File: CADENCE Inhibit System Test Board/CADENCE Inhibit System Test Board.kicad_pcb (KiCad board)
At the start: 2 copper layers, 70 x 95 mm, 61 parts, among them IC1 LTC7004IMSE#WTRPBF, IC2 LTC7004IMSE#WTRPBF, IC3 LTC7004IMSE#WTRPBF, IC4 LTC7004IMSE#WTRPBF, IC5 LTC7004IMSE#WTRPBF, J1 INHIBIT_P2, J10 Conn_01x04, J11 Conn_01x02, J2 INHIBIT_P2, J3 INHIBIT_P2, J4 INHIBIT_P2, J5 INHIBIT_P2, J6 INHIBIT_P2, J7 INHIBIT_P2, J8 INHIBIT_P2, J9 INHIBIT_P2, Q1 SUD23N06-31-GE3, Q2 SUD23N06-31-GE3, Q3 SUD23N06-31-GE3, Q4 SUD23N06-31-GE3, Q5 SUD23N06-31-GE3, Q6 SUD23N06-31-GE3, Q7 SUD23N06-31-GE3, U1 MIC4427YM-TR, U2 MIC4427YM-TR

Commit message: made pcb smaller
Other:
- board size 70 x 95 mm -> 70 x 68.6 mm
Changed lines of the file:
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@@
 		)
 		(property "Value" "LTC7004IMSE#WTRPBF"
-			(at 1.5 -0.24 90)
+			(at -0.6556 -0.24 90)
 			(unlocked yes)
 			(layer "F.Fab")
@@
 		(tags "connector Hirose DF11 vertical")
 		(property "Reference" "J5"
-			(at 1 -4.2 90)
+			(at 1 -2.5 90)
 			(layer "F.SilkS")
 			(effects
@@
 		(tags "connector Hirose DF11 vertical")
 		(property "Reference" "J1"
-			(at 6.9652 -30.2127 90)
+			(at 1 -2.5 90)
 			(layer "F.SilkS")
 			(effects
@@
 	(gr_rect
 		(start 120.465637 42.411896)
-		(end 190.465637 137.411896)
+		(end 190.465637 111)
 		(stroke
 			(width 0.2)

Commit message: mounting holes added
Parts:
- added H1: MountingHole, MountingHole:MountingHole_3.2mm_M3, F.Cu at (124.5, 43.0)
- added H2: MountingHole, MountingHole:MountingHole_3.2mm_M3, F.Cu at (186.5, 43.5)
- added H3: MountingHole, MountingHole:MountingHole_3.2mm_M3, F.Cu at (193.5, 113.0)
- added H4: MountingHole, MountingHole:MountingHole_3.2mm_M3, F.Cu at (125.0, 106.5)
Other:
- board size 70 x 68.6 mm -> 70 x 72.5 mm

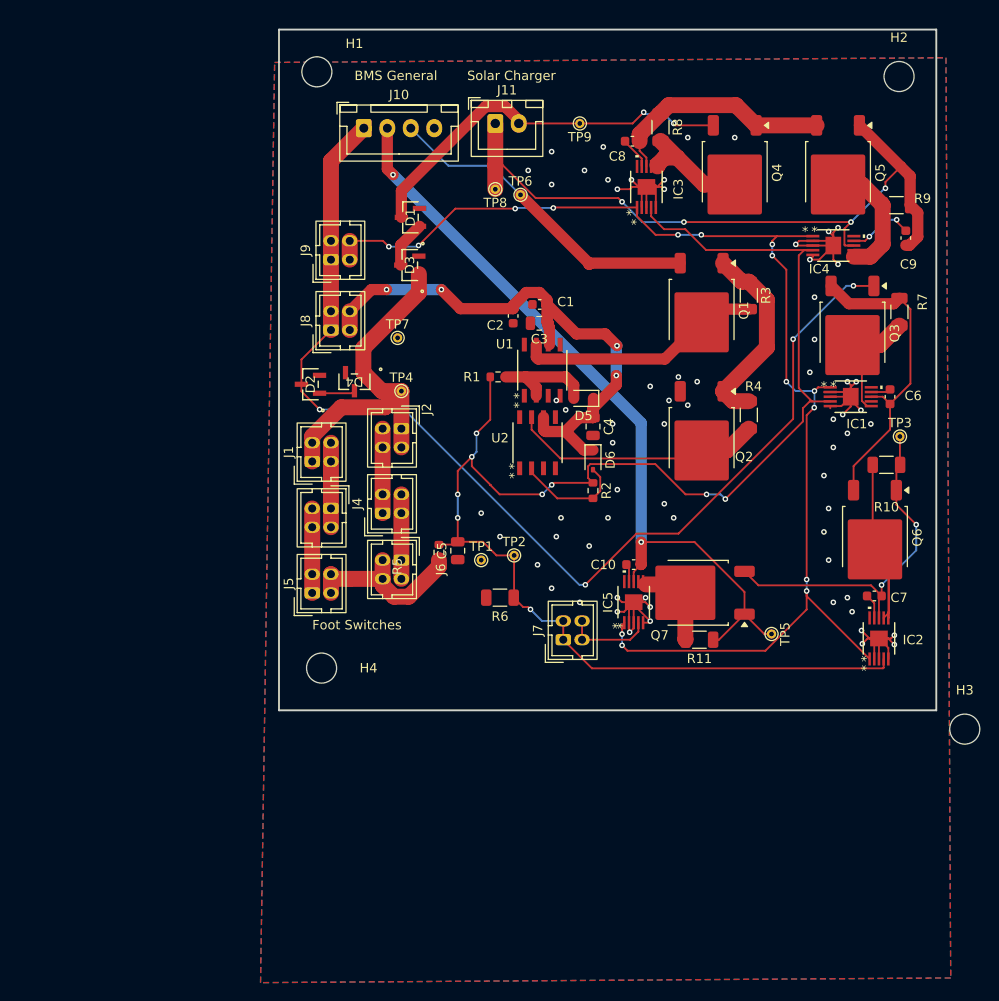
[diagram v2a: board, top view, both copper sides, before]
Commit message: moved parts and updated mounting holes
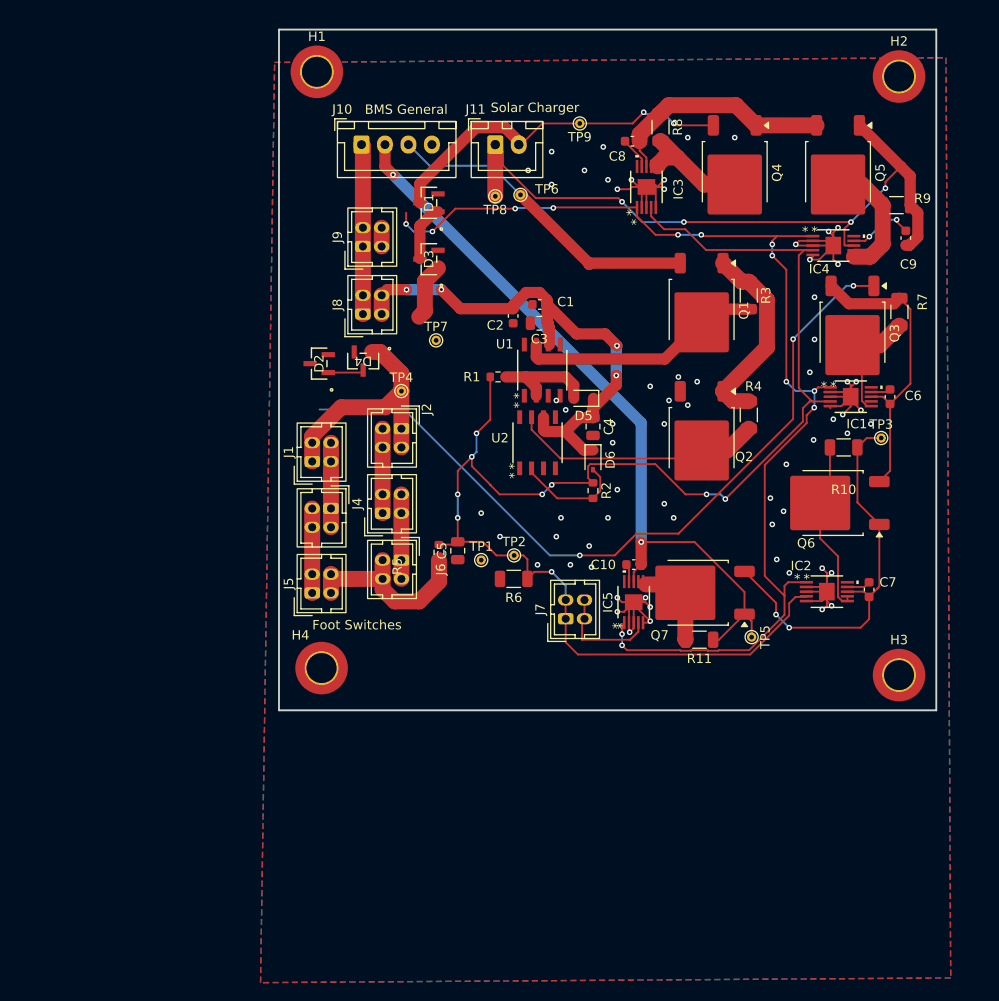
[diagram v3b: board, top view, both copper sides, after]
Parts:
- H1, H2, H3, H4: value MountingHole -> MountingHole_Pad; footprint MountingHole:MountingHole_3.2mm_M3 -> MountingHole:MountingHole_3.2mm_M3_DIN965_Pad_TopOnly
- moved H3 9.06 mm to (186.5, 107.2)
- moved IC2 7.46 mm to (178.8, 98.4), turned to 0 degrees
- moved Q6 5.87 mm to (179.4, 88.9), turned to 180 degrees
- moved R10 4.92 mm to (180.6, 83.0)
- moved TP7 4.11 mm to (137.2, 71.6)
- moved J8 3.80 mm to (129.4, 68.8)
- moved J9 3.68 mm to (129.4, 61.6)
- moved D1 2.50 mm to (136.4, 57.0)
- moved R6 2.48 mm to (145.5, 97.0)
- moved D4 2.39 mm to (129.4, 73.8)
- moved D2 2.39 mm to (124.7, 74.1)
- moved J11 2.25 mm to (143.5, 50.8)
- moved J7 2.25 mm to (151.0, 101.2)
- moved TP5 2.15 mm to (170.8, 103.2)
- moved D3 2.13 mm to (136.4, 63.0)
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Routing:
- net Cell 1+: track 118.4 -> 100.5 mm, vias 4 -> 3
- net HIGH_SIDE_PWR: track 134.6 -> 123.4 mm, vias 15 -> 13
- net Net-(D3-K): track 38.0 -> 32.1 mm
- net EN: track 164.7 -> 159.9 mm
- net Net-(IC2-TS): track 37.8 -> 42.1 mm
- net LOW_SIDE_PWR: track 62.0 -> 57.9 mm
- net V_mppt_i: track 41.8 -> 38.7 mm
- net Net-(IC2-TGDN): track 23.1 -> 20.1 mm
- net UNREG: track 83.6 -> 81.0 mm
- net Net-(IC1-TS): track 34.9 -> 32.9 mm
- net Net-(IC5-INP): track 9.30 -> 11.3 mm
- net Net-(J5-Pin_2): track 18.9 -> 20.5 mm
- net Net-(D1-K): track 4.96 -> 6.02 mm
- net VSS: track 82.0 -> 82.9 mm, vias 67 -> 66

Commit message: edited layout and rerouted traces
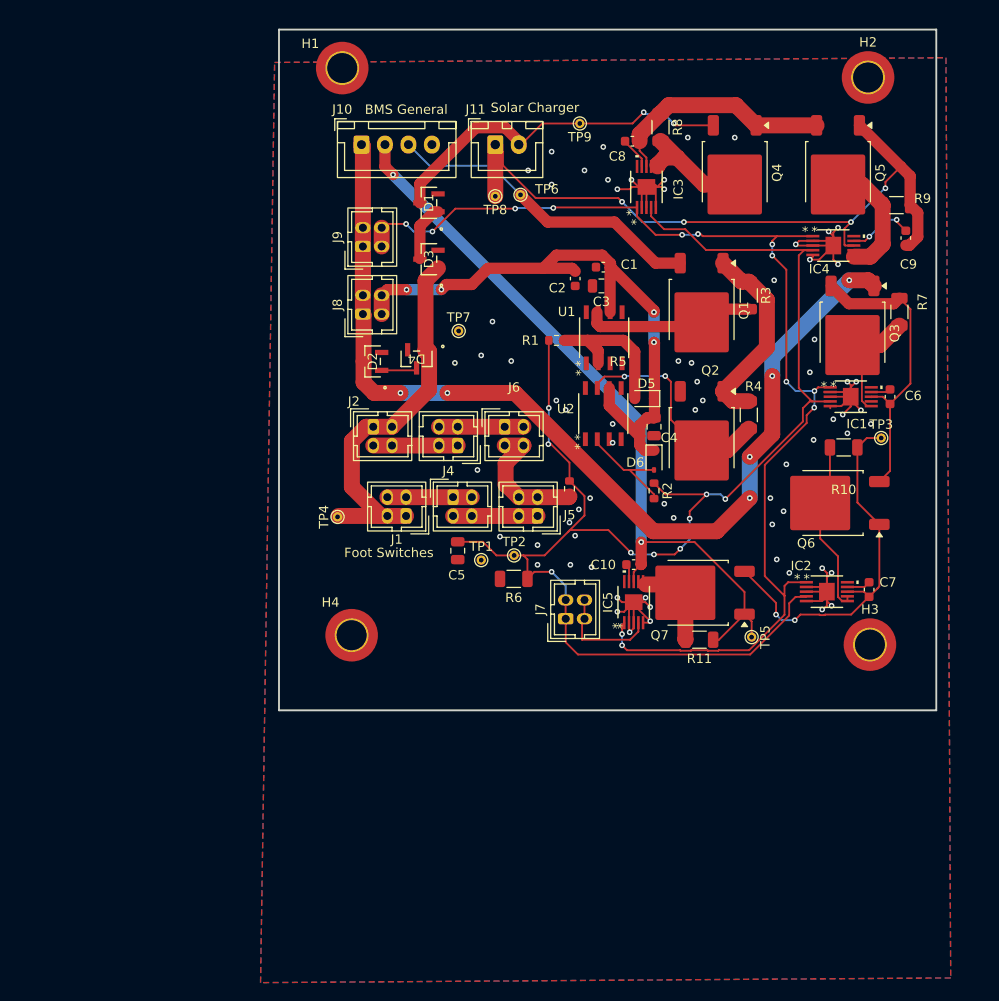
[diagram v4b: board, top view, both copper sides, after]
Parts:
- moved J5 25.4 mm to (148.0, 90.3), turned to 180 degrees
- moved J6 18.0 mm to (144.5, 80.8), turned to 0 degrees
- moved R5 15.5 mm to (151.4, 87.4)
- moved TP4 15.0 mm to (126.7, 90.4), turned to 90 degrees
- moved J3 13.1 mm to (139.0, 88.3), turned to 0 degrees
- moved J1 11.6 mm to (134.0, 90.3), turned to 180 degrees
- moved J4 10.8 mm to (139.5, 82.8), turned to 180 degrees
- moved C1 7.85 mm to (155.0, 63.8)
- moved C3 7.71 mm to (154.8, 65.8)
- moved C2 7.71 mm to (152.0, 65.0)
- moved U2 7.66 mm to (155.0, 79.4)
- moved U1 7.44 mm to (155.1, 71.3)
- moved R1 7.35 mm to (150.0, 71.6)
- moved C4 6.50 mm to (160.4, 80.8)
- moved D5 6.50 mm to (159.4, 77.8)
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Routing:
- net Cell 1+: track 100.5 -> 112.3 mm, vias 3 -> 6
- net LOW_SIDE_PWR: track 57.9 -> 67.4 mm
- net Net-(D3-K): track 32.1 -> 41.5 mm
- net Net-(Q1-G): track 26.2 -> 18.3 mm
- net Net-(J5-Pin_2): track 20.5 -> 14.4 mm
- net Net-(D5-A): track 11.5 -> 15.9 mm
- net Net-(Q2-G): track 27.1 -> 24.8 mm, vias 0 -> 2
- net EN: track 159.9 -> 162.2 mm
- net Net-(IC2-TS): track 42.1 -> 40.1 mm
- net HIGH_SIDE_PWR: track 123.4 -> 125.1 mm
- net VSS: vias 66 -> 69

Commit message: edited diode footprints
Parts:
- moved D2 2.00 mm to (128.6, 74.6)
- moved D3 0.87 mm to (135.6, 63.0)
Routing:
- net Net-(D2-K): track 3.45 -> 6.42 mm, vias 0 -> 2
- net V_mppt_i: track 38.7 -> 37.0 mm
- net Cell 1+: track 112.3 -> 111.2 mm
- net Net-(D3-K): track 41.5 -> 40.9 mm
- net VSS: vias 69 -> 89

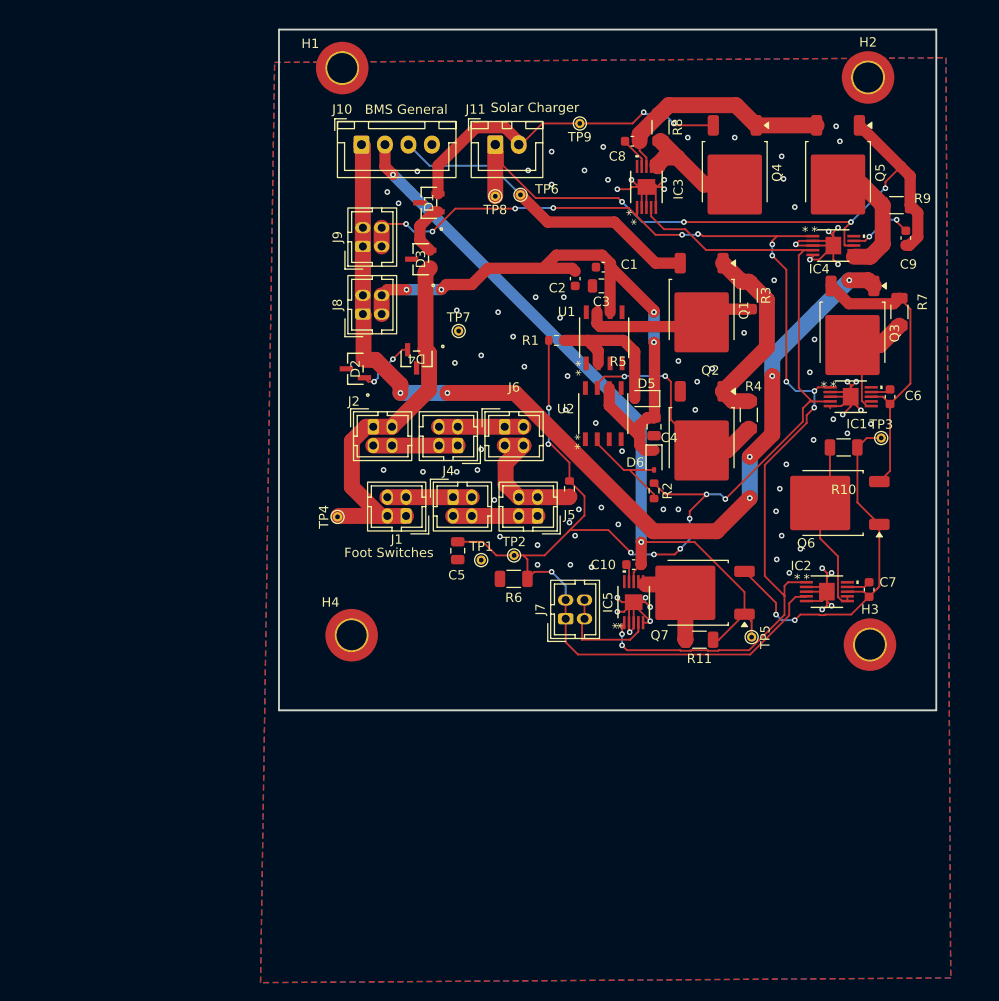
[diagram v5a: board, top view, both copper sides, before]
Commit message: Added names and vias
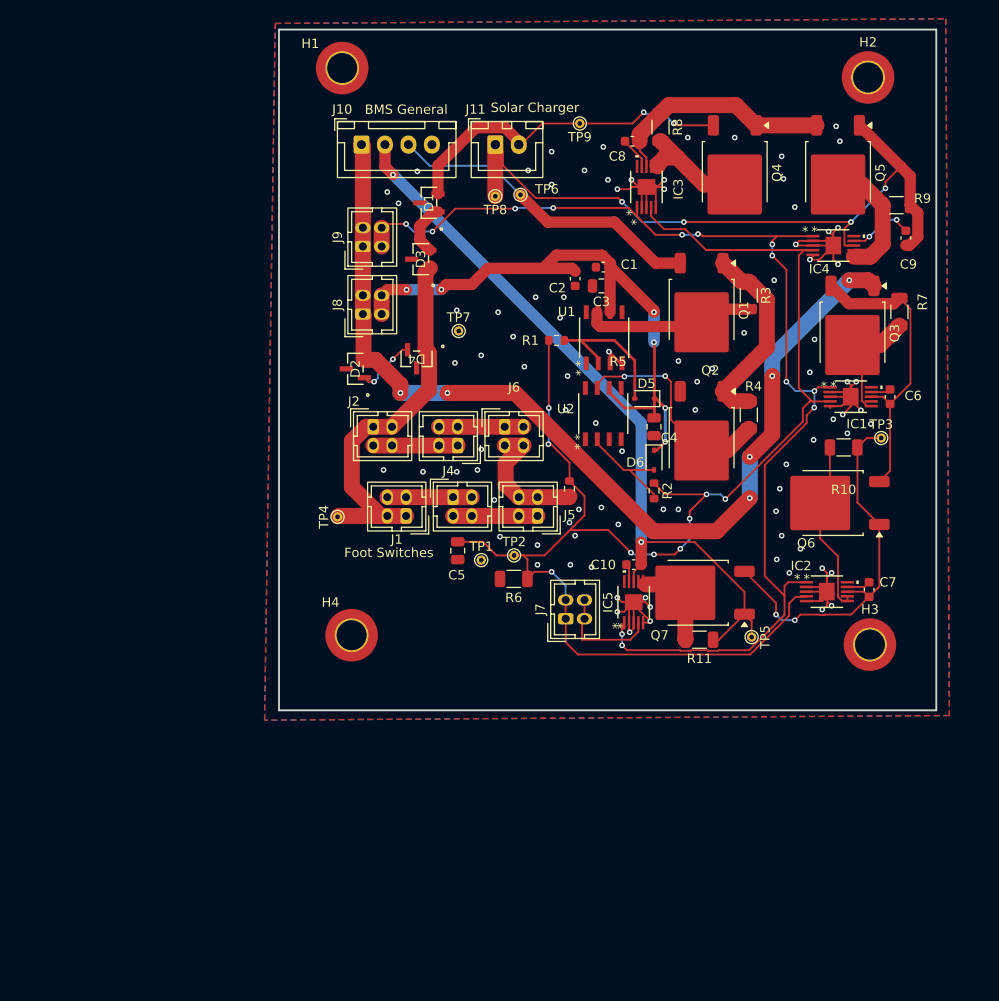
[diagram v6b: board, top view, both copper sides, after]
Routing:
- net VSS: track 82.9 -> 86.1 mm, vias 89 -> 90
- net LOW_SIDE_PWR: track 67.4 -> 68.0 mm, vias 4 -> 6
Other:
- board text added: "Made By: Helena M. and Braeden F."
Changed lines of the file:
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@@
 		(layer "Edge.Cuts")
 	)
+	(gr_text "Made By: \nHelena M. and Braeden F. "
+		(at 133.8 44 0)
+		(layer "F.Mask")
+		(effects
+			(font
+				(size 1 1)
+				(thickness 0.15)
+			)
+			(justify left bottom)
+		)
+	)
 	(gr_text "Foot Switches"
 		(at 127.4 94.8 0)
@@
 	)
 	(segment
+		(start 155.73 74.0483)
+		(end 155.73 72.93)
+		(width 0.300387)
+		(layer "F.Cu")
+		(net "VSS")
+	)
+	(segment
 		(start 176.6297 97.860301)
 		(end 178.814099 97.860301)
@@
 	)
 	(segment
+		(start 156.8483 74.0483)
+		(end 155.6 72.8)
+		(width 0.300387)
+		(layer "F.Cu")
+		(net "VSS")
+	)
+	(segment
 		(start 159.02 99.48)
 		(end 159.5 99)
@@
 	)
 	(segment
+		(start 155.73 72.93)
+		(end 155.6 72.8)
+		(width 0.300387)
+		(layer "F.Cu")
+		(net "VSS")
+	)
+	(segment
 		(start 177.3156 61.000001)
 		(end 175.874999 61.000001)
@@
 	)
 	(segment
+		(start 157 74.0483)
+		(end 156.8483 74.0483)
+		(width 0.300387)
+		(layer "F.Cu")
+		(net "VSS")
+	)
+	(segment
 		(start 177.3156 61.5)
 		(end 175.625 61.5)
@@
 	)
 	(via
+		(at 155.6 72.8)
+		(size 0.6)
+		(drill 0.3)
+		(layers "F.Cu" "B.Cu")
+		(net "VSS")
+	)
+	(via
 		(at 174.5 84.8)
 		(size 0.6)
@@
 	)
 	(segment
-		(start 159.68 79.85)
-		(end 160.405 79.85)
-		(width 1.2)
-		(layer "F.Cu")
-		(net "LOW_SIDE_PWR")
-	)
-	(segment
-		(start 158.88 82.73855)
-		(end 158.88 81.8)
-		(width 1.2)
-		(layer "F.Cu")
-		(net "LOW_SIDE_PWR")
-	)
-	(segment
 		(start 150 62.525)
 		(end 148.6 63.925)
@@
 	)
 	(segment
-		(start 158.88 80.65)
-		(end 159.68 79.85)
-		(width 1.2)
-		(layer "F.Cu")
-		(net "LOW_SIDE_PWR")
-	)
-	(segment
-		(start 160.455 77.8)
-		(end 160.455 79.8)
-		(width 1.2)
+		(start 160.455 79.8)
+		(end 160.405 79.85)
+		(width 0.300387)
 		(layer "F.Cu")
 		(net "LOW_SIDE_PWR")
@@
 	)
 	(segment
-		(start 160.455 79.8)
-		(end 160.405 79.85)
-		(width 1.2)
-		(layer "F.Cu")
-		(net "LOW_SIDE_PWR")
-	)
-	(segment
 		(start 160.4 68.425)
 		(end 155.775 63.8)
@@
 	)
 	(segment
-		(start 155.73 63.845)
-		(end 155.775 63.8)
-		(width 1.2)
+		(start 160.6 77.8)
+		(end 161.6 78.8)
+		(width 0.300387)
 		(layer "F.Cu")
 		(net "LOW_SIDE_PWR")
 	)
 	(segment
-		(start 159.44145 83.3)
-		(end 158.88 82.73855)
+		(start 155.73 63.845)
+		(end 155.775 63.8)
 		(width 1.2)
 		(layer "F.Cu")
@@
 	)
 	(segment
-		(start 154.880804 62.525)
-		(end 150 62.525)
-		(width 1.2)
+		(start 160.455 78.8)
+		(end 160.455 79.8)
+		(width 0.300387)
 		(layer "F.Cu")
 		(net "LOW_SIDE_PWR")
 	)
 	(segment
-		(start 155.635 78.555)
-		(end 158.88 81.8)
+		(start 154.880804 62.525)
+		(end 150 62.525)
 		(width 1.2)
 		(layer "F.Cu")
@@
 	)
 	(segment
-		(start 160.455 71.855)
-		(end 160.4 71.8)
-		(width 1.2)
+		(start 160.455 77.8)
+		(end 160.455 78.8)
+		(width 0.300387)
 		(layer "F.Cu")
 		(net "LOW_SIDE_PWR")
@@
 	)
 	(segment
-		(start 155.635 76.67585)
-		(end 155.635 78.555)
-		(width 1.2)
+		(start 157.2956 78.8)
+		(end 160.455 78.8)
+		(width 0.300387)
 		(layer "F.Cu")
 		(net "LOW_SIDE_PWR")
@@
 	)
 	(segment
-		(start 158.88 81.8)
-		(end 158.88 80.65)
-		(width 1.2)
+		(start 155.635 77.1394)
+		(end 157.2956 78.8)
+		(width 0.300387)
 		(layer "F.Cu")
 		(net "LOW_SIDE_PWR")
@@
 	)
 	(segment
+		(start 155.635 76.67585)
+		(end 155.635 77.1394)
+		(width 0.300387)
+		(layer "F.Cu")
+		(net "LOW_SIDE_PWR")
+	)
+	(segment
 		(start 141 65.65)
 		(end 138.3 65.65)
@@
 	)
 	(segment
-		(start 160.405 83.3)
-		(end 159.44145 83.3)
-		(width 1.2)
+		(start 160.455 77.8)
+		(end 160.455 71.855)
+		(width 0.300387)
+		(layer "F.Cu")
+		(net "LOW_SIDE_PWR")
+	)
+	(segment
+		(start 160.7 83.3)
+		(end 160.405 83.3)
+		(width 0.300387)
+		(layer "F.Cu")
+		(net "LOW_SIDE_PWR")
+	)
+	(segment
+		(start 161.6 82.4)
+		(end 160.7 83.3)
+		(width 0.300387)
 		(layer "F.Cu")
 		(net "LOW_SIDE_PWR")
@@
 	(segment
 		(start 160.455 77.8)
-		(end 160.455 71.855)
-		(width 1.2)
+		(end 160.6 77.8)
+		(width 0.300387)
 		(layer "F.Cu")
 		(net "LOW_SIDE_PWR")
 	)
+	(segment
+		(start 160.455 71.855)
+		(end 160.4 71.8)
+		(width 0.300387)
+		(layer "F.Cu")
+		(net "LOW_SIDE_PWR")
+	)
+	(via
+		(at 161.6 82.4)
+		(size 0.6)
+		(drill 0.3)
+		(layers "F.Cu" "B.Cu")
+		(net "LOW_SIDE_PWR")
+	)
 	(via
 		(at 137.76 66.19)
@@
 	)
 	(via
+		(at 161.6 78.8)
+		(size 0.6)
+		(drill 0.3)
+		(layers "F.Cu" "B.Cu")
+		(net "LOW_SIDE_PWR")
+	)
+	(via
 		(at 160.4 71.8)
 		(size 0.6)
@@
 	)
 	(segment
+		(start 161.6 82.4)
+		(end 161.6 78.8)
+		(width 0.300387)
+		(layer "B.Cu")
+		(net "LOW_SIDE_PWR")
+	)
+	(segment
 		(start 160.4 71.8)
 		(end 160.4 68.6)
@@
 	)
 	(segment
-		(start 158.355 72.80635)
-		(end 158.355 77.8)
-		(width 1.2)
+		(start 154.46 74.0483)
+		(end 154.46 73.46)
+		(width 0.300387)
 		(layer "F.Cu")
 		(net "Net-(D5-A)")
 	)
 	(segment
-		(start 154.46 72.72135)
-		(end 153.33865 71.6)
-		(width 1.2)
+		(start 158.355 73.755)
+		(end 158.355 77.8)
+		(width 0.300387)
 		(layer "F.Cu")
 		(net "Net-(D5-A)")
 	)
 	(segment
-		(start 153.33865 71.6)
-		(end 157.14865 71.6)
-		(width 1.2)
+		(start 150.85 71.6)
+		(end 152.6 71.6)
+		(width 0.300387)
 		(layer "F.Cu")
 		(net "Net-(D5-A)")
 	)
 	(segment
-		(start 154.46 74.0483)
-		(end 154.46 72.72135)
-		(width 1.2)
+		(start 154.46 73.46)
+		(end 152.6 71.6)
+		(width 0.300387)
 		(layer "F.Cu")
 		(net "Net-(D5-A)")
 	)
 	(segment
-		(start 157.14865 71.6)
-		(end 158.355 72.80635)
-		(width 1.2)
+		(start 156.2 71.6)
+		(end 158.355 73.755)
+		(width 0.300387)
 		(layer "F.Cu")
 		(net "Net-(D5-A)")
 	)
 	(segment
-		(start 150.85 71.6)
-		(end 153.33865 71.6)
-		(width 1.2)
+		(start 152.6 71.6)
+		(end 156.2 71.6)
+		(width 0.300387)
 		(layer "F.Cu")
 		(net "Net-(D5-A)")
@@
 		(polygon
 			(pts
-				(xy 120 42) (xy 191.5 41.5) (xy 192 139.5) (xy 118.5 140)
+				(xy 120.063522 37.849906) (xy 191.478829 37.350498) (xy 191.857408 111.551991) (xy 118.927835 112.04811)
 			)
 		)

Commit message: grounded mounting holes
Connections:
- H1 pad 1: unconnected-(H1-Pad1) -> VSS
- H2 pad 1: unconnected-(H2-Pad1) -> VSS
- H3 pad 1: unconnected-(H3-Pad1) -> VSS
- H4 pad 1: unconnected-(H4-Pad1) -> VSS
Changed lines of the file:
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@@
 			(layers "*.Cu" "*.Mask")
 			(remove_unused_layers no)
-			(net "unconnected-(H4-Pad1)")
+			(net "VSS")
 			(pinfunction "1_1")
 			(pintype "input")
@@
 			(size 5.6 5.6)
 			(layers "F.Cu" "F.Mask")
-			(net "unconnected-(H4-Pad1)")
+			(net "VSS")
 			(pinfunction "1_1")
 			(pintype "input")
@@
 			(layers "*.Cu" "*.Mask")
 			(remove_unused_layers no)
-			(net "unconnected-(H1-Pad1)")
+			(net "VSS")
 			(pinfunction "1_1")
 			(pintype "input")
@@
 			(size 5.6 5.6)
 			(layers "F.Cu" "F.Mask")
-			(net "unconnected-(H1-Pad1)")
+			(net "VSS")
 			(pinfunction "1_1")
 			(pintype "input")
@@
 			(layers "*.Cu" "*.Mask")
 			(remove_unused_layers no)
-			(net "unconnected-(H3-Pad1)")
+			(net "VSS")
 			(pinfunction "1_1")
 			(pintype "input")
@@
 			(size 5.6 5.6)
 			(layers "F.Cu" "F.Mask")
-			(net "unconnected-(H3-Pad1)")
+			(net "VSS")
 			(pinfunction "1_1")
 			(pintype "input")
@@
 		(sheetname "/")
 		(sheetfile "CADENCE Inhibit System Test Board.kicad_sch")
+		(units
+			(unit
+				(name "A")
+				(pins "1" "2")
+			)
+		)
 		(attr smd)
 		(duplicate_pad_numbers_are_jumpers no)
@@
 		(sheetname "/")
 		(sheetfile "CADENCE Inhibit System Test Board.kicad_sch")
+		(units
+			(unit
+				(name "A")
+				(pins "1" "2")
+			)
+		)
 		(attr smd)
 		(duplicate_pad_numbers_are_jumpers no)
@@
 		(sheetname "/")
 		(sheetfile "CADENCE Inhibit System Test Board.kicad_sch")
+		(units
+			(unit
+				(name "A")
+				(pins "1" "2")
+			)
+		)
 		(attr smd)
 		(duplicate_pad_numbers_are_jumpers no)
@@
 			(layers "*.Cu" "*.Mask")
 			(remove_unused_layers no)
-			(net "unconnected-(H2-Pad1)")
+			(net "VSS")
 			(pinfunction "1_1")
 			(pintype "input")
@@
 			(size 5.6 5.6)
 			(layers "F.Cu" "F.Mask")
-			(net "unconnected-(H2-Pad1)")
+			(net "VSS")
 			(pinfunction "1_1")
 			(pintype "input")
@@
 		(sheetname "/")
 		(sheetfile "CADENCE Inhibit System Test Board.kicad_sch")
+		(units
+			(unit
+				(name "A")
+				(pins "1" "2")
+			)
+		)
 		(attr smd)
 		(duplicate_pad_numbers_are_jumpers no)
